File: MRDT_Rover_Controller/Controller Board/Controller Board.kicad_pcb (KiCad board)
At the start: 2 copper layers, 137.6 x 81.5 mm, 29 parts, among them Q1 S8050, U1 MCP3008

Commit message: PCB Updated
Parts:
- added SW1: EG1218, digikey-footprints:Switch_Slide_11.6x4mm_EG1218, F.Cu at (191.0, 55.2)
- renumbered S3 to S1, S4 to S3, S1 to S4
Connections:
- BAT1 pad POS: Net-(5V_Regulator1-Pad1) -> Net-(BAT1-PadPOS)
- R11 pad 2: SW3 -> SW1
- R12 pad 2: SW4 -> SW3
- R9 pad 2: SW1 -> SW4
- S1 pad 4: SW3 -> SW1
- S3 pad 4: SW4 -> SW3
- S4 pad 4: SW1 -> SW4
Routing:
- net SW4: track 3.48 -> 90.3 mm
- net SW3: track 10.9 -> 95.6 mm
- net SW2: track 9.04 -> 88.1 mm
- net Net-(BAT1-PadPOS): track 0.00 -> 43.7 mm, vias 0 -> 1
- net Net-(5V_Regulator1-Pad1): track 44.9 -> 21.1 mm
- net SW1: track 76.7 -> 72.0 mm, vias 0 -> 1
- net 5V: track 346.4 -> 342.3 mm, vias 1 -> 3
- net GND: vias 4 -> 1

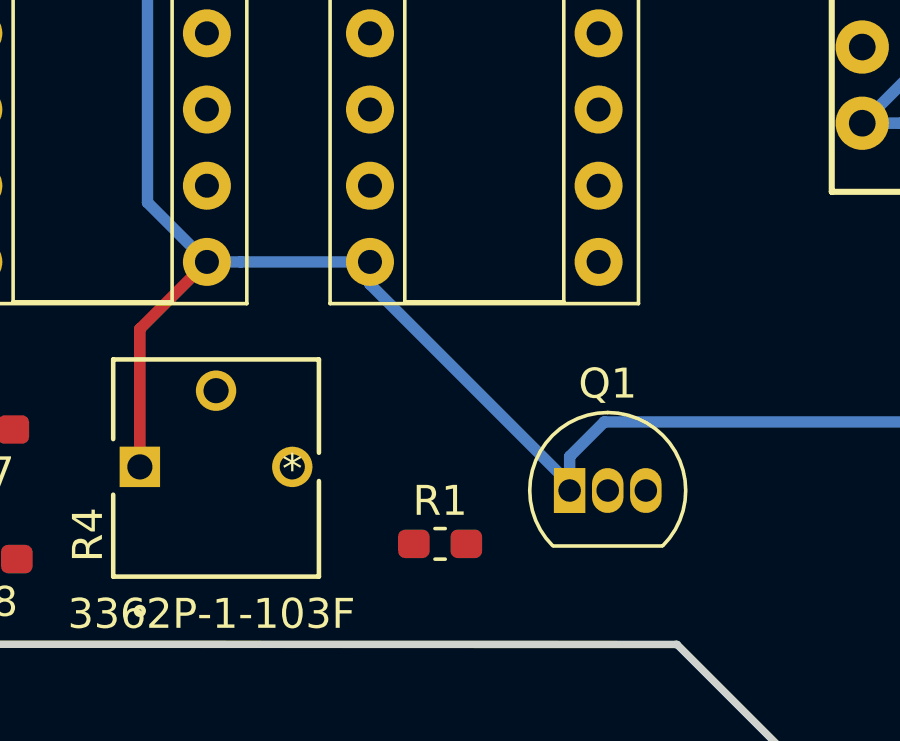
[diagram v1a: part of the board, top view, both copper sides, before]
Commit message: PCB Updated, Power Switch Added
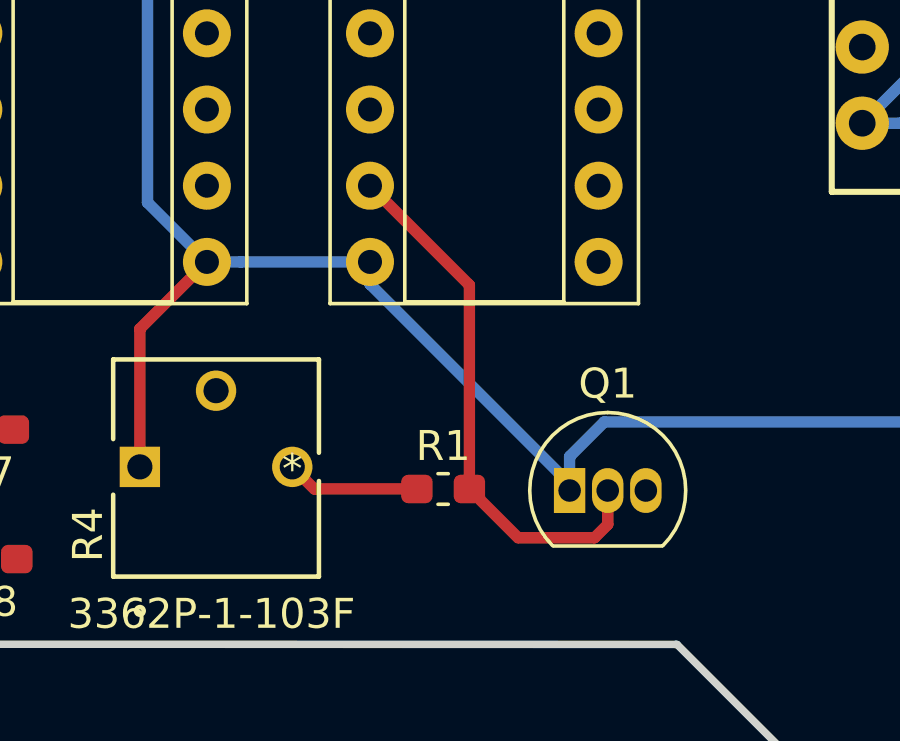
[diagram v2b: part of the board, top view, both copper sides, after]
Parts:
- moved R1 1.83 mm to (175.0, 119.4)
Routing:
- net /P3: track 0.00 -> 18.1 mm
- net 5V: track 342.3 -> 346.8 mm
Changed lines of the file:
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@@
     (thickness 1.6)
     (drawings 25)
-    (tracks 243)
+    (tracks 251)
     (zones 0)
     (modules 30)
@@
   )
   (module Resistor_SMD:R_0603_1608Metric_Pad1.05x0.95mm_HandSolder (layer F.Cu)
-    (at 174.9044 121.2088)
+    (at 175.006 119.38)
     (descr "Resistor SMD 0603 (1608 Metric), square (rectangular) end terminal, IPC_7351 nominal with elongated pad for handsoldering. (Body size source: http://www.tortai-tech.com/upload/download/2011102023233369053.pdf), generated with kicad-footprint-generator")
     (tags "resistor handsolder")
@@
   (segment (start 180.5546 99.4778) (end 180.1876 99.1108) (width 0.381) (layer F.Cu) (net 36))
   (segment (start 185.0644 99.4778) (end 180.5546 99.4778) (width 0.381) (layer F.Cu) (net 36))
+  (segment (start 175.881 112.5842) (end 175.881 119.38) (width 0.381) (layer F.Cu) (net 40))
+  (segment (start 172.5676 109.2708) (end 175.881 112.5842) (width 0.381) (layer F.Cu) (net 40))
+  (segment (start 180.4924 120.5618) (end 180.0486 121.0056) (width 0.381) (layer F.Cu) (net 40))
+  (segment (start 180.4924 119.4308) (end 180.4924 120.5618) (width 0.381) (layer F.Cu) (net 40))
+  (segment (start 177.5066 121.0056) (end 175.881 119.38) (width 0.381) (layer F.Cu) (net 40))
+  (segment (start 180.0486 121.0056) (end 177.5066 121.0056) (width 0.381) (layer F.Cu) (net 40))
   (segment (start 83.82 59.817) (end 83.693 59.69) (width 0.381) (layer F.Cu) (net 43))
   (segment (start 83.82 64.149) (end 83.82 59.817) (width 0.381) (layer F.Cu) (net 43))
@@
   (segment (start 211.328 97.732315) (end 207.7212 94.125515) (width 0.381) (layer B.Cu) (net 66))
   (segment (start 211.328 98.298) (end 211.328 97.732315) (width 0.381) (layer B.Cu) (net 66))
+  (segment (start 170.7134 119.38) (end 169.9768 118.6434) (width 0.381) (layer F.Cu) (net 66))
+  (segment (start 174.131 119.38) (end 170.7134 119.38) (width 0.381) (layer F.Cu) (net 66))
   (segment (start 184.904 67.056) (end 186.2836 67.056) (width 0.381) (layer B.Cu) (net 67))
   (segment (start 186.2836 67.056) (end 186.2836 67.056) (width 0.381) (layer B.Cu) (net 67))

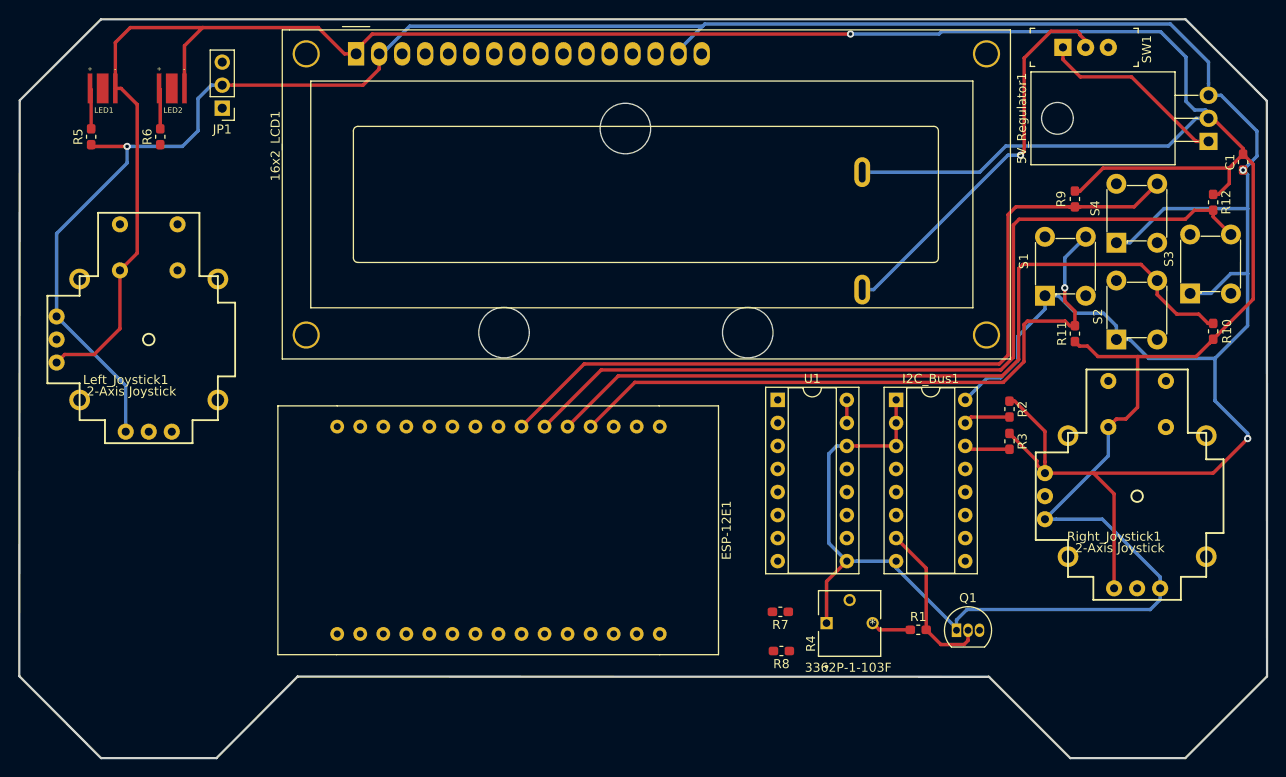
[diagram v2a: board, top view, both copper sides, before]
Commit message: I2C Traces Placed
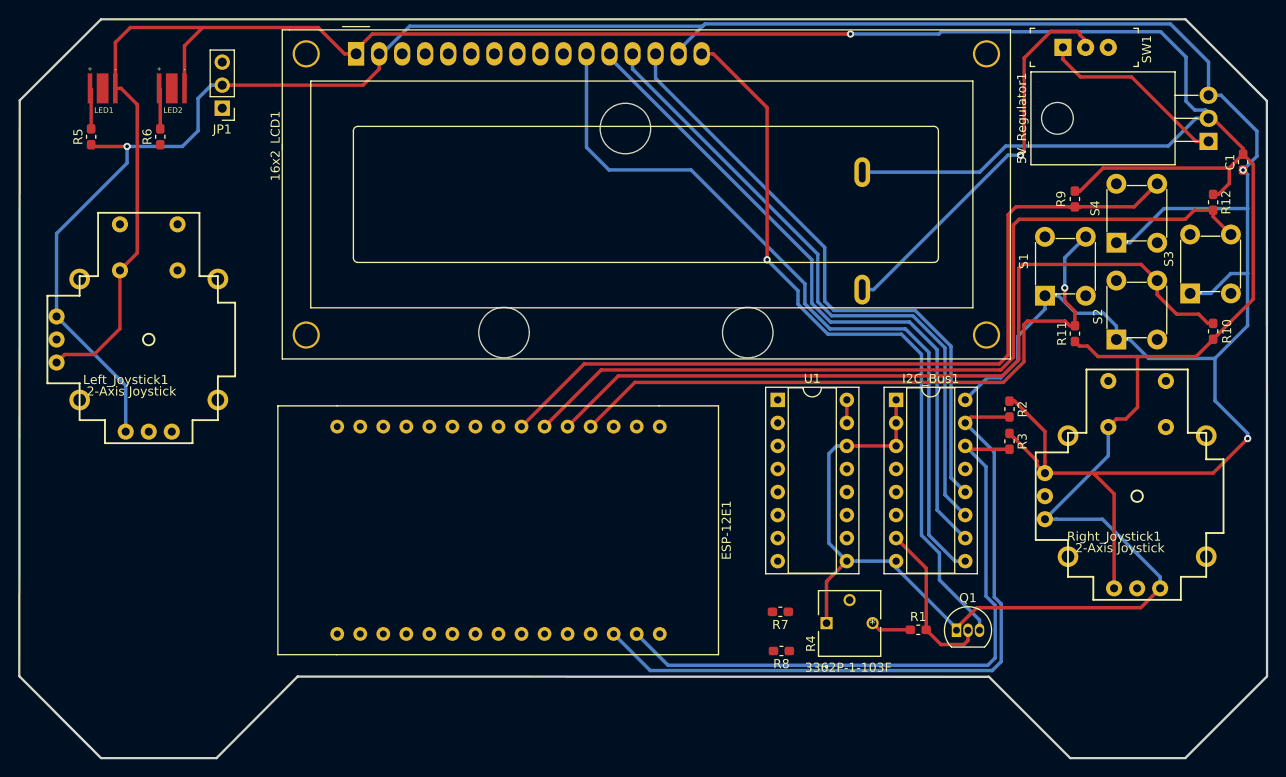
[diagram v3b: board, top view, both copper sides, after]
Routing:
- net Net-(16x2_LCD1-Pad11): track 0.00 -> 84.1 mm
- net /k: track 0.00 -> 81.7 mm, vias 0 -> 1
- net Net-(16x2_LCD1-Pad12): track 0.00 -> 74.7 mm
- net SDA: track 5.15 -> 77.9 mm
- net Net-(16x2_LCD1-Pad13): track 0.00 -> 71.3 mm
- net Net-(16x2_LCD1-Pad14): track 0.00 -> 67.7 mm
- net SCL: track 5.03 -> 71.1 mm
- net GND: track 404.9 -> 403.6 mm

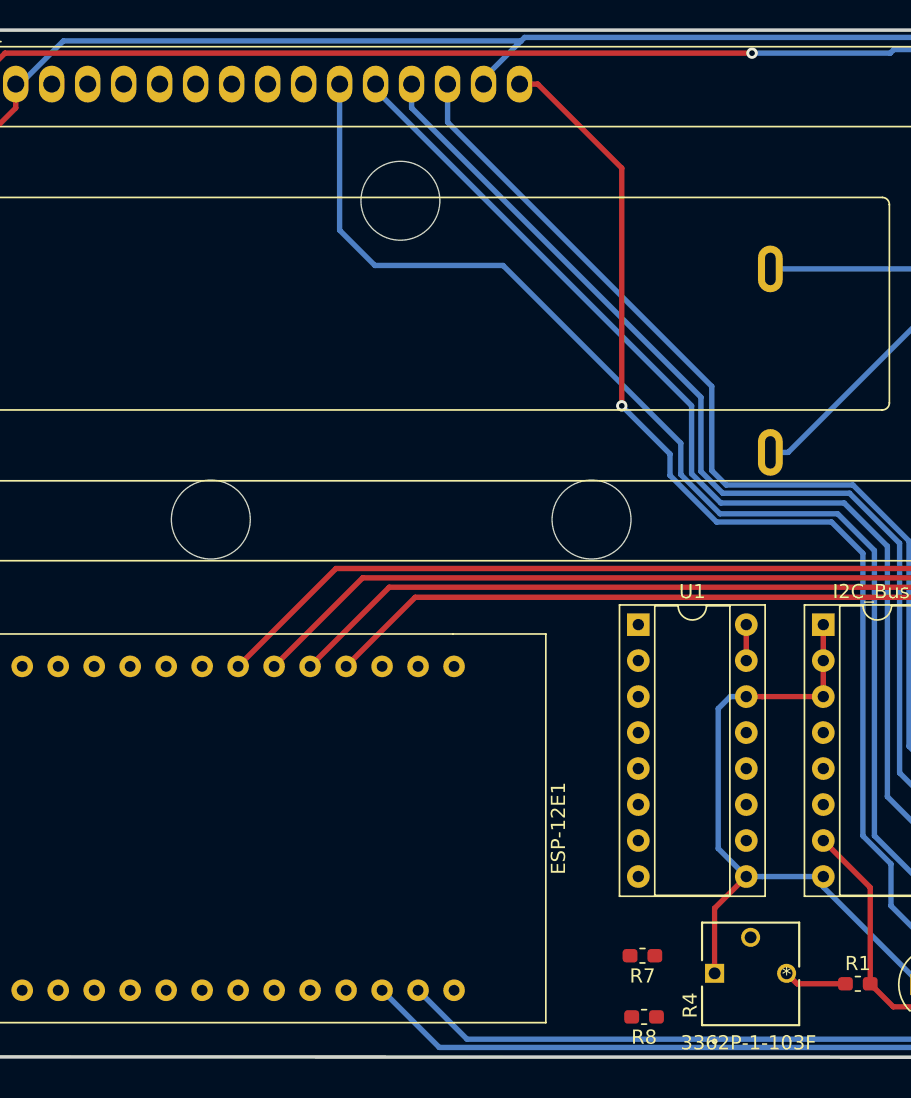
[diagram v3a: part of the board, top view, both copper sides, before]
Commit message: All I2C Traces Placed
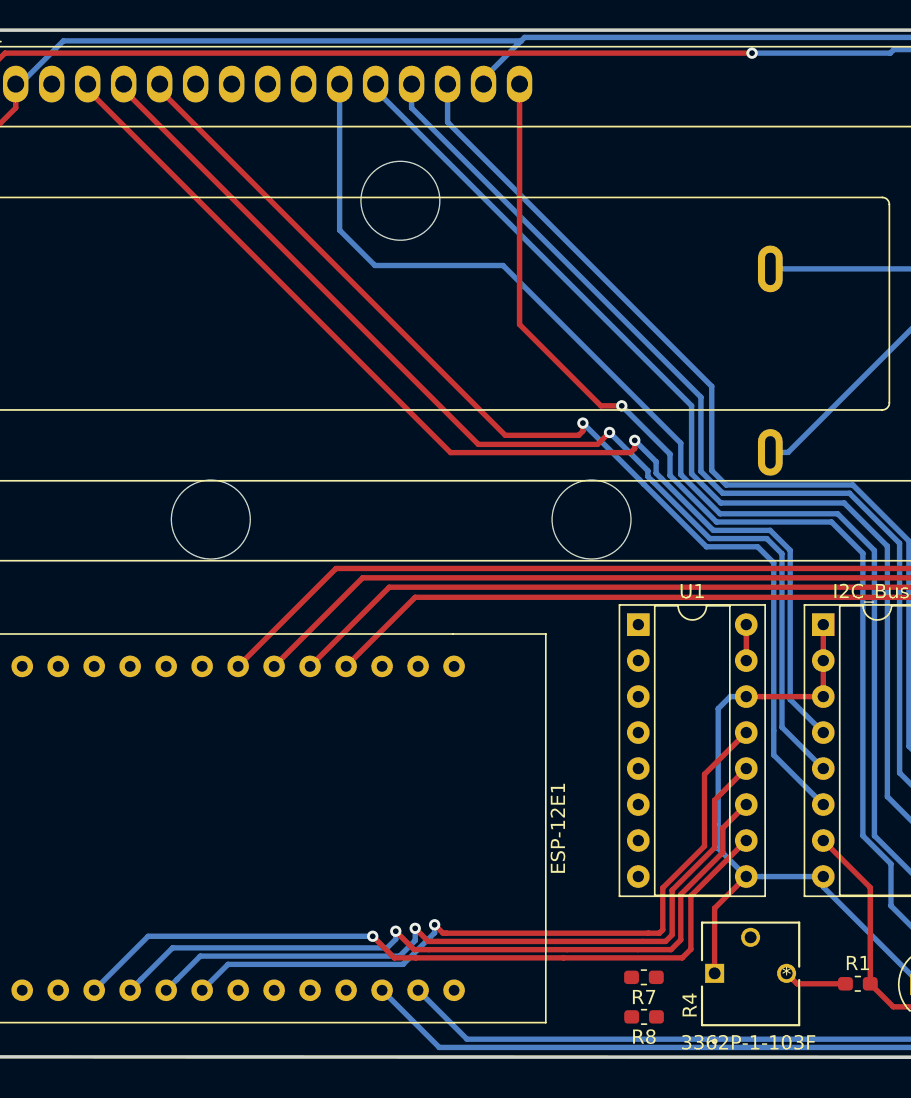
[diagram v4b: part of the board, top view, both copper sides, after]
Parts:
- moved R7 1.53 mm to (159.9, 118.9)
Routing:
- net Net-(16x2_LCD1-Pad4): track 0.00 -> 78.8 mm, vias 0 -> 1
- net Net-(16x2_LCD1-Pad5): track 0.00 -> 77.7 mm, vias 0 -> 1
- net Net-(16x2_LCD1-Pad6): track 0.00 -> 77.1 mm, vias 0 -> 1
- net CS: track 0.00 -> 53.9 mm, vias 0 -> 1
- net Din: track 0.00 -> 53.2 mm, vias 0 -> 1
- net Dout: track 0.00 -> 52.5 mm, vias 0 -> 1
- net CLK: track 0.00 -> 51.5 mm, vias 0 -> 1

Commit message: PCB Updated
Team Lead approved design at this point.
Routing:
- net V0: track 0.00 -> 86.9 mm
- net RGHT_SEL: track 0.00 -> 44.2 mm, vias 0 -> 1
- net 5V: track 346.8 -> 386.3 mm
- net RightVert: track 0.00 -> 17.6 mm, vias 0 -> 1
- net RightHorz: track 0.00 -> 14.9 mm, vias 0 -> 1
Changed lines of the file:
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@@
     (thickness 1.6)
     (drawings 25)
-    (tracks 419)
+    (tracks 460)
     (zones 0)
     (modules 30)
@@
   (segment (start 159.258 81.591685) (end 158.960085 81.8896) (width 0.381) (layer F.Cu) (net 12))
   (segment (start 159.258 81.026) (end 159.258 81.591685) (width 0.381) (layer F.Cu) (net 12))
+  (segment (start 163.972313 112.638913) (end 163.972313 91.500887) (width 0.381) (layer B.Cu) (net 13))
+  (segment (start 167.4368 116.1034) (end 163.972313 112.638913) (width 0.381) (layer B.Cu) (net 13))
+  (segment (start 163.972313 91.500887) (end 163.047826 90.5764) (width 0.381) (layer B.Cu) (net 13))
+  (segment (start 118.11 56.28) (end 118.11 55.88) (width 0.381) (layer B.Cu) (net 13))
+  (segment (start 152.4064 90.5764) (end 118.11 56.28) (width 0.381) (layer B.Cu) (net 13))
+  (segment (start 163.047826 90.5764) (end 152.4064 90.5764) (width 0.381) (layer B.Cu) (net 13))
   (segment (start 168.83 68.924) (end 181.774 68.924) (width 0.381) (layer B.Cu) (net 14))
   (segment (start 181.774 68.924) (end 184.658 66.04) (width 0.381) (layer B.Cu) (net 14))
@@
   (segment (start 91.44 59.817) (end 91.313 59.69) (width 0.381) (layer F.Cu) (net 45))
   (segment (start 91.44 64.149) (end 91.44 59.817) (width 0.381) (layer F.Cu) (net 45))
+  (segment (start 187.718765 104.648) (end 186.0296 106.337165) (width 0.381) (layer B.Cu) (net 48))
+  (segment (start 188.976 104.648) (end 187.718765 104.648) (width 0.381) (layer B.Cu) (net 48))
+  (segment (start 186.0296 106.337165) (end 186.0296 120.2944) (width 0.381) (layer B.Cu) (net 48))
+  (segment (start 186.0296 120.2944) (end 186.0296 120.2944) (width 0.381) (layer B.Cu) (net 48))
+  (via (at 186.0296 120.2944) (size 0.8) (drill 0.4) (layers F.Cu B.Cu) (net 48))
+  (segment (start 199.136 116.065235) (end 197.040435 118.1608) (width 0.381) (layer B.Cu) (net 49))
+  (segment (start 199.136 114.808) (end 199.136 116.065235) (width 0.381) (layer B.Cu) (net 49))
+  (segment (start 197.040435 118.1608) (end 196.1388 118.1608) (width 0.381) (layer B.Cu) (net 49))
+  (segment (start 196.1388 118.1608) (end 189.1284 118.1608) (width 0.381) (layer B.Cu) (net 49))
+  (segment (start 189.1284 118.1608) (end 187.1472 120.142) (width 0.381) (layer B.Cu) (net 49))
+  (segment (start 187.1472 120.142) (end 187.1472 120.142) (width 0.381) (layer B.Cu) (net 49))
+  (via (at 187.1472 120.142) (size 0.8) (drill 0.4) (layers F.Cu B.Cu) (net 49))
+  (segment (start 195.961 93.205235) (end 203.5556 100.799835) (width 0.381) (layer B.Cu) (net 53))
+  (segment (start 195.961 91.948) (end 195.961 93.205235) (width 0.381) (layer B.Cu) (net 53))
+  (segment (start 203.5556 100.799835) (end 203.5556 116.7892) (width 0.381) (layer B.Cu) (net 53))
+  (segment (start 203.5556 116.7892) (end 201.4728 118.872) (width 0.381) (layer B.Cu) (net 53))
+  (segment (start 201.4728 118.872) (end 199.0852 118.872) (width 0.381) (layer B.Cu) (net 53))
+  (segment (start 199.0852 118.872) (end 196.2404 118.872) (width 0.381) (layer B.Cu) (net 53))
+  (segment (start 196.2404 118.872) (end 189.8904 118.872) (width 0.381) (layer B.Cu) (net 53))
+  (segment (start 189.8904 118.872) (end 188.6712 120.0912) (width 0.381) (layer B.Cu) (net 53))
+  (segment (start 188.6712 120.0912) (end 188.6712 120.0912) (width 0.381) (layer B.Cu) (net 53))
+  (via (at 188.6712 120.0912) (size 0.8) (drill 0.4) (layers F.Cu B.Cu) (net 53))
   (segment (start 192.853 72.757) (end 192.8644 72.7456) (width 0.381) (layer F.Cu) (net 54))
   (segment (start 192.278 72.757) (end 192.853 72.757) (width 0.381) (layer F.Cu) (net 54))
@@
   (segment (start 185.6394 94.1718) (end 188.976 97.5084) (width 0.381) (layer F.Cu) (net 66))
   (segment (start 185.0644 94.1718) (end 185.6394 94.1718) (width 0.381) (layer F.Cu) (net 66))
-  (segment (start 167.132 94.0308) (end 167.132 96.5708) (width 0.381) (layer F.Cu) (net 66))
   (segment (start 148.59 55.48) (end 148.59 55.88) (width 0.381) (layer B.Cu) (net 66))
   (segment (start 151.238 52.832) (end 148.59 55.48) (width 0.381) (layer B.Cu) (net 66))
@@
   (segment (start 170.7134 119.38) (end 169.9768 118.6434) (width 0.381) (layer F.Cu) (net 66))
   (segment (start 174.131 119.38) (end 170.7134 119.38) (width 0.381) (layer F.Cu) (net 66))
+  (segment (start 169.9768 116.417542) (end 167.148058 113.5888) (width 0.381) (layer B.Cu) (net 66))
+  (segment (start 169.9768 118.6434) (end 169.9768 116.417542) (width 0.381) (layer B.Cu) (net 66))
+  (segment (start 167.148058 113.5888) (end 166.6748 113.5888) (width 0.381) (layer B.Cu) (net 66))
+  (segment (start 166.332001 97.370799) (end 167.132 96.5708) (width 0.381) (layer B.Cu) (net 66))
+  (segment (start 164.56979 99.13301) (end 166.332001 97.370799) (width 0.381) (layer B.Cu) (net 66))
+  (segment (start 164.56979 111.48379) (end 164.56979 99.13301) (width 0.381) (layer B.Cu) (net 66))
+  (segment (start 166.6748 113.5888) (end 164.56979 111.48379) (width 0.381) (layer B.Cu) (net 66))
+  (segment (start 160.7934 118.9342) (end 160.782 118.9228) (width 0.381) (layer F.Cu) (net 66))
+  (segment (start 160.7934 121.7168) (end 160.7934 118.9342) (width 0.381) (layer F.Cu) (net 66))
+  (segment (start 161.4184 121.7168) (end 160.7934 121.7168) (width 0.381) (layer F.Cu) (net 66))
+  (segment (start 167.855307 121.7168) (end 161.4184 121.7168) (width 0.381) (layer F.Cu) (net 66))
+  (segment (start 169.9768 119.595307) (end 167.855307 121.7168) (width 0.381) (layer F.Cu) (net 66))
+  (segment (start 169.9768 118.6434) (end 169.9768 119.595307) (width 0.381) (layer F.Cu) (net 66))
+  (segment (start 167.132 96.5708) (end 167.132 94.0308) (width 0.381) (layer B.Cu) (net 66))
   (segment (start 170.086 81.874) (end 184.904 67.056) (width 0.381) (layer B.Cu) (net 67))
   (segment (start 168.83 81.874) (end 170.086 81.874) (width 0.381) (layer B.Cu) (net 67))
